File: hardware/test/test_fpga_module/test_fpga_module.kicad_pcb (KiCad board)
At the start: 2 copper layers, 2 parts, among them J1 Conn_02x26_Odd_Even, J2 Conn_02x26_Odd_Even

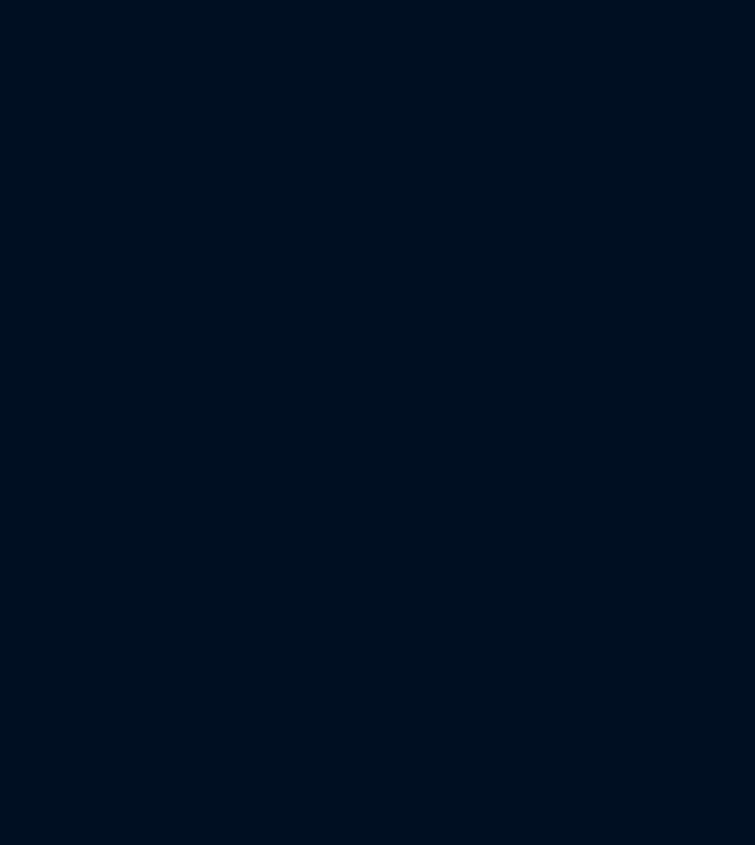
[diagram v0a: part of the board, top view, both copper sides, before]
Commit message: busses added
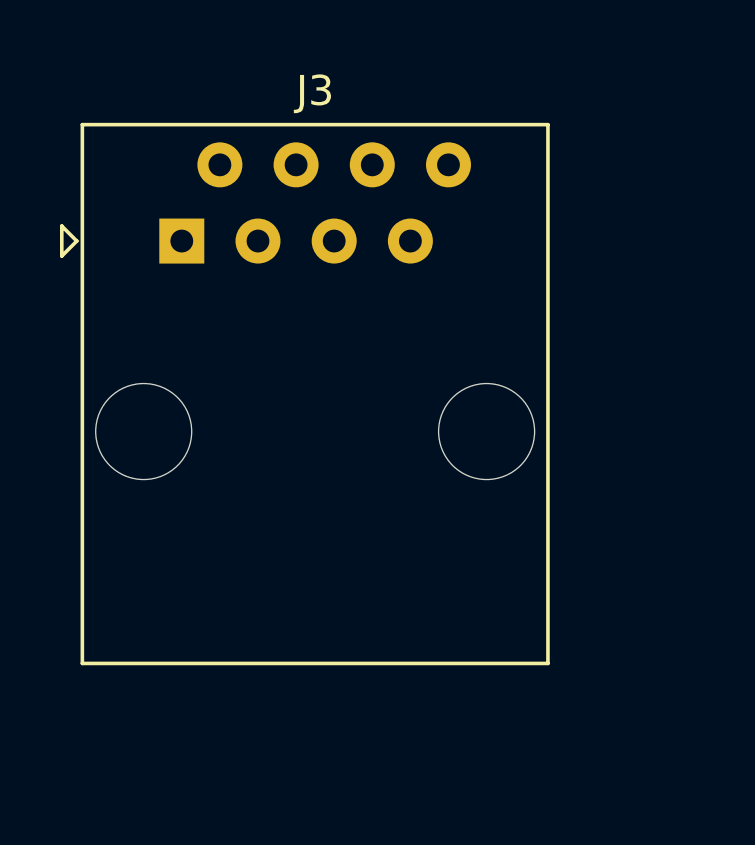
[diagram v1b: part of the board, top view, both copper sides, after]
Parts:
- added J3: 8P8C, Connector_RJ:RJ45_Amphenol_54602-x08_Horizontal, F.Cu at (-39.6, -30.9)
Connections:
- J1 pad 23: Net-(J1-Pad23) -> /A8
- J1 pad 25: Net-(J1-Pad25) -> /A7
- J1 pad 27: Net-(J1-Pad27) -> /A6
- J1 pad 29: Net-(J1-Pad29) -> /A5
- J1 pad 31: Net-(J1-Pad31) -> /A4
- J1 pad 33: Net-(J1-Pad33) -> /A3
- J1 pad 35: Net-(J1-Pad35) -> /A2
- J1 pad 37: Net-(J1-Pad37) -> /A1
